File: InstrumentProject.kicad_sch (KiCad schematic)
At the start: 1 part, among them U2 STM32F103RET6TR

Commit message: I haven't been making any commits, but I have been making progress on adding symbols and beginning connections
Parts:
- removed U2: STM32F103RET6TR, STM32:QFP50P1200X1200X160-64N, symbol STM32:STM32F103RET6TR
- added J1: USB4105-GF-A, USB4105-GF-A:GCT_USB4105-GF-A, symbol USB:USB4105-GF-A
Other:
- added sheet CODEC (CODEC.kicad_sch)
- added sheet IO (IO.kicad_sch)
- added sheet MCU (MCU.kicad_sch)
- added sheet Power (Power.kicad_sch)
- note added: "Top Level"
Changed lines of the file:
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@@
 (kicad_sch (version 20230121) (generator eeschema)
   (paper "A4")
-  (symbol (lib_name "STM32F103RET6TR_1") (lib_id "STM32:STM32F103RET6TR") (at 140.97 92.71 0) (unit 1)
+  (text "Top Level" (at 15.24 25.4 0)
+    (effects (font (face "Calibri") (size 7.62 7.62) (thickness 1.524) bold) (justify left bottom))
+  )
+  (symbol (lib_id "USB:USB4105-GF-A") (at 190.5 129.54 0) (unit 1)
     (in_bom yes) (on_board yes) (dnp no) (fields_autoplaced)
-    (property "Reference" "U2" (at 140.97 24.13 0)
+    (property "Reference" "J1" (at 201.93 96.52 0)
       (effects (font (size 1.27 1.27)))
     )
-    (property "Value" "STM32F103RET6TR" (at 140.97 26.67 0)
+    (property "Value" "USB4105-GF-A" (at 201.93 99.06 0)
       (effects (font (size 1.27 1.27)))
     )
-    (property "Footprint" "STM32:QFP50P1200X1200X160-64N" (at 140.97 92.71 0)
+    (property "Footprint" "USB4105-GF-A:GCT_USB4105-GF-A" (at 172.72 123.19 0)
       (effects (font (size 1.27 1.27)) (justify bottom) hide)
     )
-    (property "Datasheet" "" (at 140.97 92.71 0)
+    (property "Datasheet" "" (at 205.74 104.14 0)
       (effects (font (size 1.27 1.27)) hide)
     )
-    (property "STANDARD" "IPC-7351B" (at 140.97 92.71 0)
+    (property "PARTREV" "B3" (at 172.72 118.11 0)
       (effects (font (size 1.27 1.27)) (justify bottom) hide)
     )
-    (property "MANUFACTURER" "STMicroelectronics" (at 140.97 92.71 0)
+    (property "MANUFACTURER" "Global Connector Technology" (at 170.18 125.73 0)
       (effects (font (size 1.27 1.27)) (justify bottom) hide)
     )
-    (pin "1")
-    (pin "10")
-    (pin "11")
-    (pin "12")
-    (pin "13")
-    (pin "14")
-    (pin "15")
-    (pin "16")
-    (pin "17")
-    (pin "18")
-    (pin "19")
-    (pin "2")
-    (pin "20")
-    (pin "21")
-    (pin "22")
-    (pin "23")
-    (pin "24")
-    (pin "25")
-    (pin "26")
-    (pin "27")
-    (pin "28")
-    (pin "29")
-    (pin "3")
-    (pin "30")
-    (pin "31")
-    (pin "32")
-    (pin "33")
-    (pin "34")
-    (pin "35")
-    (pin "36")
-    (pin "37")
-    (pin "38")
-    (pin "39")
-    (pin "4")
-    (pin "40")
-    (pin "41")
-    (pin "42")
-    (pin "43")
-    (pin "44")
-    (pin "45")
-    (pin "46")
-    (pin "47")
-    (pin "48")
-    (pin "49")
-    (pin "5")
-    (pin "50")
-    (pin "51")
-    (pin "52")
-    (pin "53")
-    (pin "54")
-    (pin "55")
-    (pin "56")
-    (pin "57")
-    (pin "58")
-    (pin "59")
-    (pin "6")
-    (pin "60")
-    (pin "61")
-    (pin "62")
-    (pin "63")
-    (pin "64")
-    (pin "7")
-    (pin "8")
-    (pin "9")
+    (property "MAXIMUM_PACKAGE_HEIGHT" "3.31mm" (at 173.99 121.92 0)
+      (effects (font (size 1.27 1.27)) (justify bottom) hide)
+    )
+    (property "STANDARD" "Manufacturer Recommendations" (at 176.53 125.73 0)
+      (effects (font (size 1.27 1.27)) (justify bottom) hide)
+    )
+    (pin "A1_B12")
+    (pin "A4_B9")
+    (pin "A5")
+    (pin "A6")
+    (pin "A7")
+    (pin "A8")
+    (pin "B1_A12")
+    (pin "B4_A9")
+    (pin "B5")
+    (pin "B6")
+    (pin "B7")
+    (pin "B8")
+    (pin "SH1")
+    (pin "SH2")
+    (pin "SH3")
+    (pin "SH4")
     (instances
       (project "InstrumentProject"
         (path "/cc59b727-2652-4091-b082-bd90d9e2c9b9"
-          (reference "U2") (unit 1)
+          (reference "J1") (unit 1)
         )
       )
     )
+  )
+  (sheet (at 176.53 44.45) (size 26.67 27.94) (fields_autoplaced)
+    (stroke (width 0.1524) (type solid))
+    (fill (color 0 0 0 0.0000))
+    (property "Sheetname" "Power" (at 176.53 43.7384 0)
+      (effects (font (size 1.27 1.27)) (justify left bottom))
+    )
+    (property "Sheetfile" "Power.kicad_sch" (at 176.53 72.9746 0)
+      (effects (font (size 1.27 1.27)) (justify left top))
+    )
+    (pin "VBUS" input (at 176.53 50.8 180)
+      (effects (font (size 1.27 1.27)) (justify left))
+    )
+    (instances
+      (project "InstrumentProject"
+        (path "/cc59b727-2652-4091-b082-bd90d9e2c9b9" (page "2"))
+      )
+    )
+  )
+  (sheet (at 114.3 82.55) (size 35.56 34.29) (fields_autoplaced)
+    (stroke (width 0.1524) (type solid) (color 0 0 0 1))
+    (fill (color 154 176 255 1.0000))
+    (property "Sheetname" "MCU" (at 114.3 81.8384 0)
+      (effects (font (size 1.27 1.27)) (justify left bottom))
+    )
+    (property "Sheetfile" "MCU.kicad_sch" (at 114.3 117.4246 0)
+      (effects (font (size 1.27 1.27)) (justify left top))
+    )
+    (instances
+      (project "InstrumentProject"
+        (path "/cc59b727-2652-4091-b082-bd90d9e2c9b9" (page "3"))
+      )
+    )
+  )
+  (sheet (at 82.55 50.8) (size 24.13 30.48) (fields_autoplaced)
+    (stroke (width 0.1524) (type solid))
+    (fill (color 0 0 0 0.0000))
+    (property "Sheetname" "CODEC" (at 82.55 50.0884 0)
+      (effects (font (size 1.27 1.27)) (justify left bottom))
+    )
+    (property "Sheetfile" "CODEC.kicad_sch" (at 82.55 81.8646 0)
+      (effects (font (size 1.27 1.27)) (justify left top))
+    )
+    (instances
+      (project "InstrumentProject"
+        (path "/cc59b727-2652-4091-b082-bd90d9e2c9b9" (page "4"))
+      )
+    )
+  )
+  (sheet (at 48.26 102.87) (size 24.13 24.13) (fields_autoplaced)
+    (stroke (width 0.1524) (type solid))
+    (fill (color 0 0 0 0.0000))
+    (property "Sheetname" "IO" (at 48.26 102.1584 0)
+      (effects (font (size 1.27 1.27)) (justify left bottom))
+    )
+    (property "Sheetfile" "IO.kicad_sch" (at 48.26 127.5846 0)
+      (effects (font (size 1.27 1.27)) (justify left top))
+    )
+    (instances
+      (project "InstrumentProject"
+        (path "/cc59b727-2652-4091-b082-bd90d9e2c9b9" (page "5"))
+      )
+    )

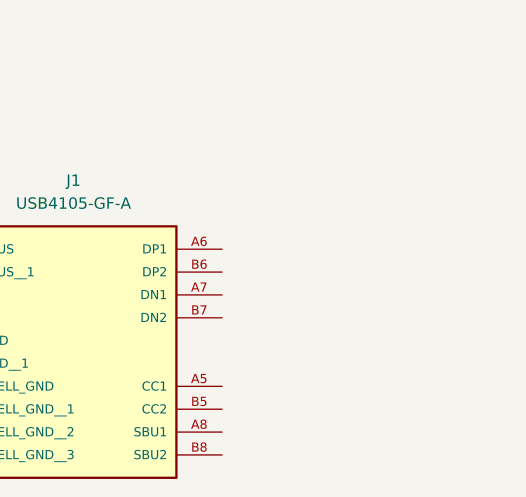
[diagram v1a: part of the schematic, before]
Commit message: Worked more on CODEC sheet, beginning symbol for new MCU part chosen
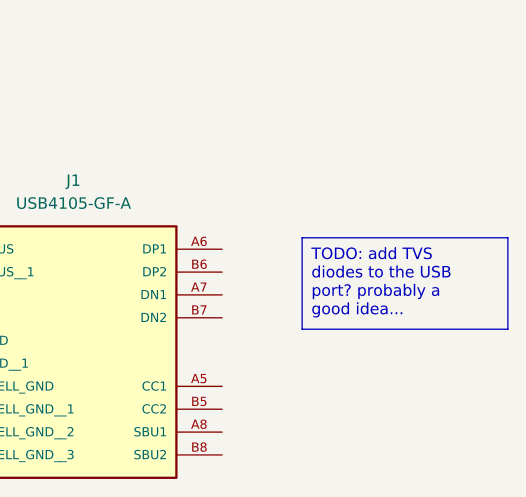
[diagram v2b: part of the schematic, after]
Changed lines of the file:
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@@
 (kicad_sch (version 20230121) (generator eeschema)
   (paper "A4")
+  (text_box "TODO: add TVS diodes to the USB port? probably a good idea..."
+    (at 227.33 102.87 0) (size 22.86 10.16)
+    (stroke (width 0) (type default))
+    (fill (type none))
+    (effects (font (size 1.27 1.27)) (justify left top))
+  )
   (text "Top Level" (at 15.24 25.4 0)
     (effects (font (face "Calibri") (size 7.62 7.62) (thickness 1.524) bold) (justify left bottom))
